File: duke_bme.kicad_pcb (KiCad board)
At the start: 2 copper layers, 101.6 x 101.6 mm, 0 parts

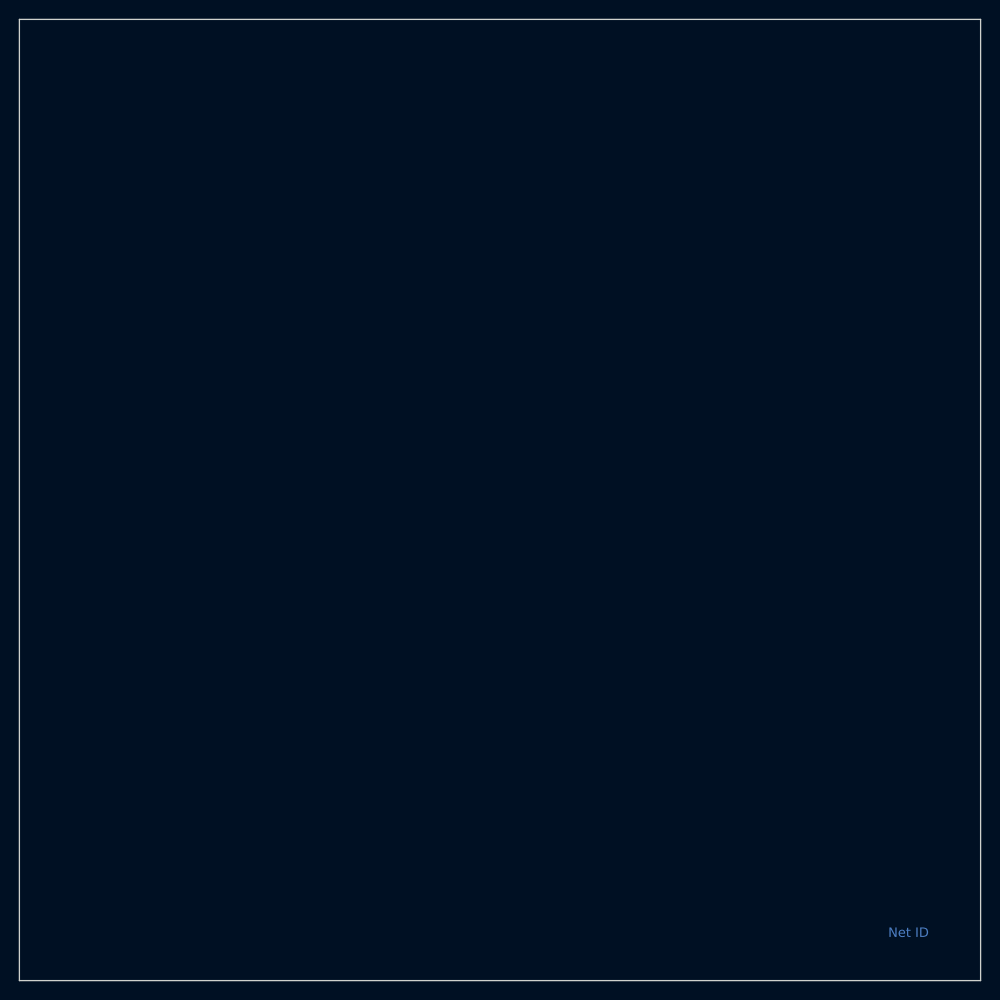
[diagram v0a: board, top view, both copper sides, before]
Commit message: add back ground pour
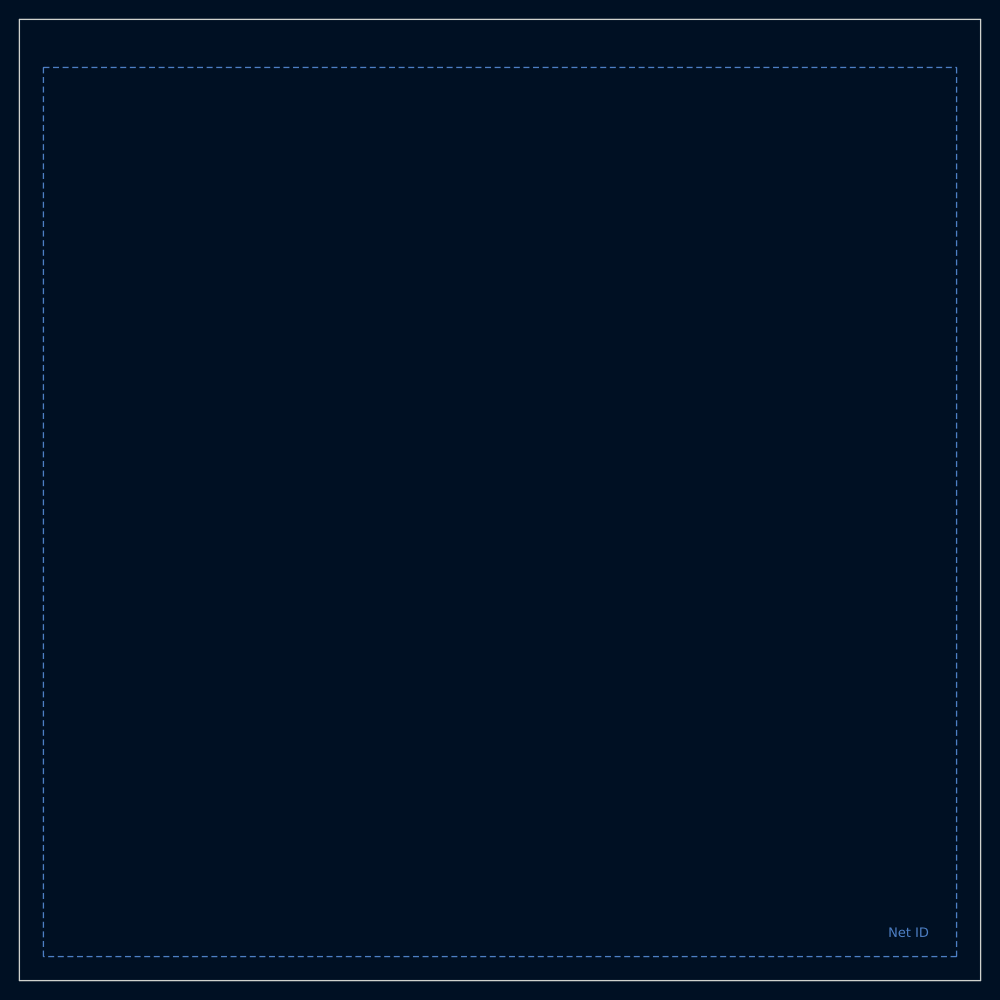
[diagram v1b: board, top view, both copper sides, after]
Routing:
- added copper zone on B.Cu, net (none)
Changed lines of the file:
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@@
     (effects (font (size 1 1) (thickness 0.15)))
   )
+  (zone (net 0) (net_name "") (layer "B.Cu") (hatch edge 0.508)
+    (connect_pads (clearance 0.508))
+    (min_thickness 0.254) (filled_areas_thickness no)
+    (fill yes (thermal_gap 0.508) (thermal_bridge_width 0.508))
+    (polygon
+      (pts
+        (xy 200.66 149.86)
+        (xy 104.14 149.86)
+        (xy 104.14 55.88)
+        (xy 200.66 55.88)
+      )
+    )
+  )
 )

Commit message: update sheet metadata
change from using text annotation tool in the sheet footers to defining
the sheet metadata using the Page Settings interface
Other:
- board text removed: "00"
- board text removed: "Duke BME Project Template"
- board text removed: "Insert Date Here"
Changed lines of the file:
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@@
   )
   (paper "A4")
+  (title_block
+    (title "BME Project Template")
+    (date "2022-02-16")
+    (rev "01")
+    (company "Mark Palmeri (Duke University)")
+  )
   (layers
     (0 "F.Cu" signal)
@@
     (effects (font (size 1 1) (thickness 0.15)))
   )
-  (gr_text "Insert Date Here" (at 213.36 193.04) (layer "User.1")
-    (effects (font (size 1 1) (thickness 0.15)))
-  )
-  (gr_text "Duke BME Project Template" (at 198.12 190.5) (layer "User.1")
-    (effects (font (size 1 1) (thickness 0.15)))
-  )
-  (gr_text "00" (at 271.78 193.04) (layer "User.1")
-    (effects (font (size 1 1) (thickness 0.15)))
-  )
